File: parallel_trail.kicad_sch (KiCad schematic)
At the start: 88 parts, among them U1 TL074, U3 TL074, U4 DG419LDY, U5 TL072, U6 PT2258

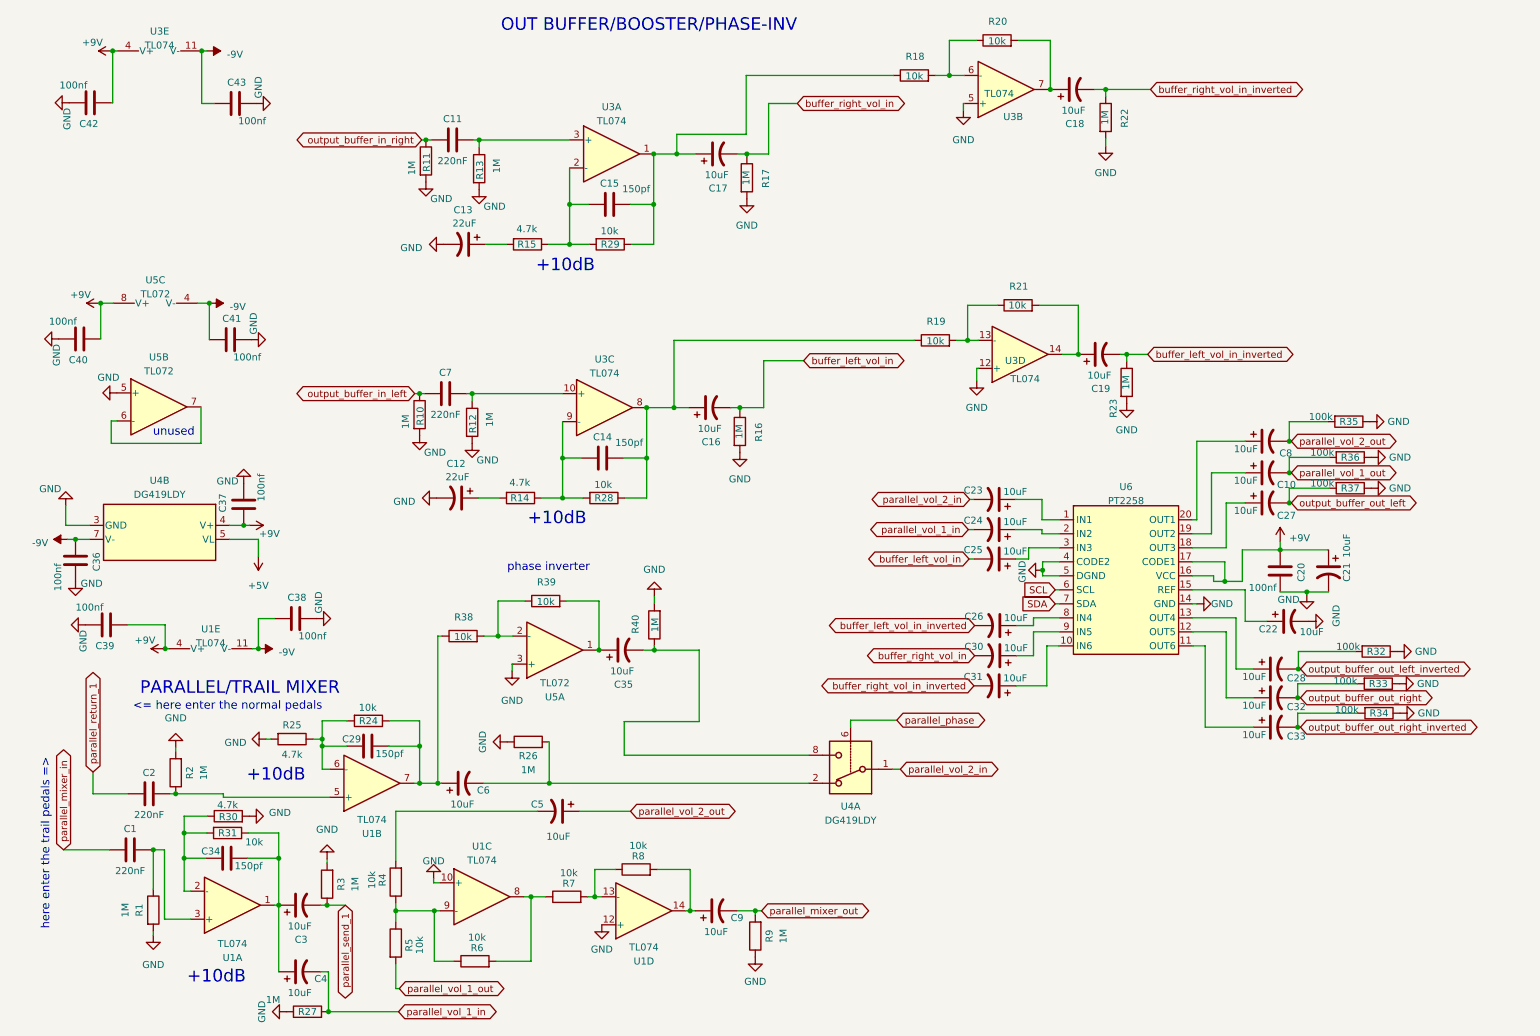
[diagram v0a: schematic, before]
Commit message: changed dg419 to 3.3V
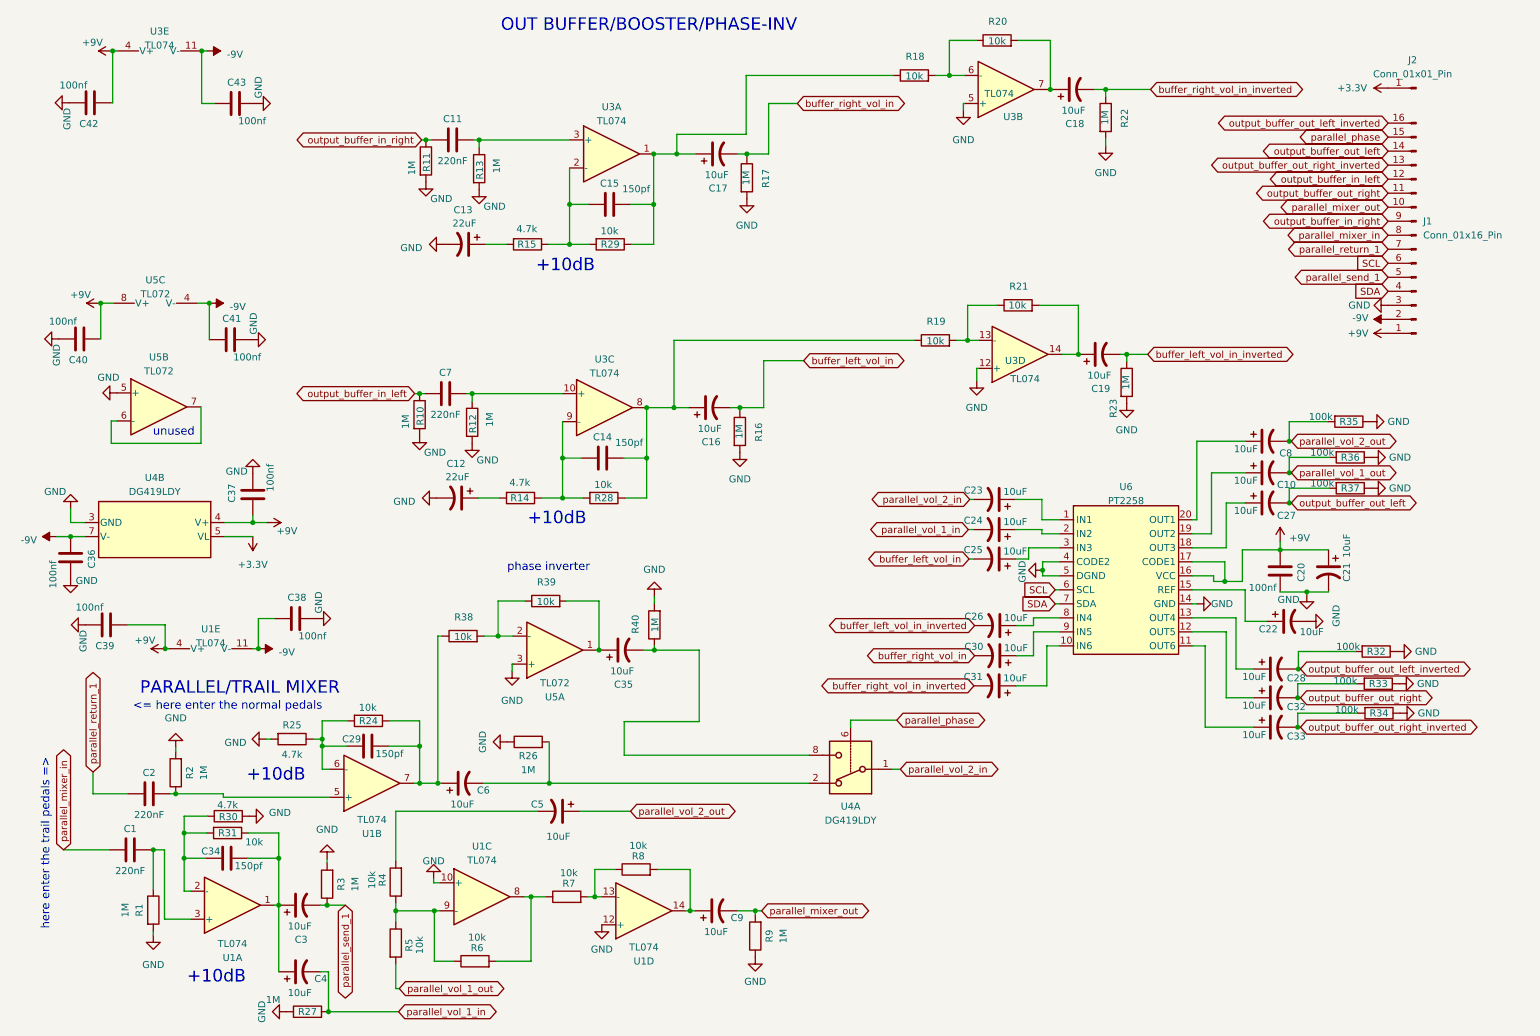
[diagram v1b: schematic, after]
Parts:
- added J1: Conn_01x16_Pin, PinHeader_2x08_P2.54mm_Vertical, symbol Connector:Conn_01x16_Pin
- added J2: Conn_01x01_Pin, Connector_PinHeader_1.00mm:PinHeader_1x01_P1.00mm_Vertical, symbol Connector:Conn_01x01_Pin
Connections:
- net +9V: now also J1.1 (Pin_1)
- net -9V: now also J1.2 (Pin_2)
- net GND: now also J1.3 (Pin_3)
- net SCL: now also J1.6 (Pin_6)
- net SDA: now also J1.4 (Pin_4)
- net output_buffer_in_left: now also J1.12 (Pin_12)
- net output_buffer_in_right: now also J1.9 (Pin_9)
- net output_buffer_out_left: now also J1.14 (Pin_14)
- net output_buffer_out_left_inverted: now also J1.16 (Pin_16)
- net output_buffer_out_right: now also J1.11 (Pin_11)
- net output_buffer_out_right_inverted: now also J1.13 (Pin_13)
- net parallel_mixer_in: now also J1.8 (Pin_8)
- net parallel_mixer_out: now also J1.10 (Pin_10)
- net parallel_phase: now also J1.15 (Pin_15)
- net parallel_return_1: now also J1.7 (Pin_7)
- net parallel_send_1: now also J1.5 (Pin_5)
- net +5V renamed +3.3V
- net +3.3V: now also J2.1 (Pin_1)
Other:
- moved on the sheet: C36, C37, U4B
